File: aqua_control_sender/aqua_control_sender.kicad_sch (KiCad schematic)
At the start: 38 parts, among them J1 USB_C, J4 Conn_01x03, J5 Conn_01x03, Q2 IRLML6402, SW1 RESET, SW2 BOOT, U1 ESP32-S3-WROOM-1, U2 LM1117-3.3, U3 RA-02_LORA

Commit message: routing completed
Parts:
- removed Q2: IRLML6402, Package_TO_SOT_SMD:SOT-23, symbol Transistor_FET:IRLML6402
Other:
- note removed: "D"
- note removed: "G"
- note removed: "Protection"
- note removed: "Reverse Polarity"
- note removed: "S"
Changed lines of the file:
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@@
 	)
 	(rectangle
-		(start 106.68 144.78)
-		(end 135.89 191.77)
-		(stroke
-			(width 0)
-			(type default)
-		)
-		(fill
-			(type none)
-		)
-	)
-	(rectangle
 		(start 45.72 96.52)
 		(end 74.93 143.51)
@@
 		)
 	)
-	(text "D"
-		(exclude_from_sim no)
-		(at 116.332 172.974 0)
-		(effects
-			(font
-				(size 1.27 1.27)
-			)
-		)
-	)
 	(text "LDO SECTION"
 		(exclude_from_sim no)
@@
 		)
 	)
-	(text "Protection"
-		(exclude_from_sim no)
-		(at 114.808 149.352 0)
-		(effects
-			(font
-				(face "Aldrich")
-				(size 1.905 1.905)
-			)
-		)
-	)
-	(text "Reverse Polarity "
-		(exclude_from_sim no)
-		(at 118.364 146.812 0)
-		(effects
-			(font
-				(face "Aldrich")
-				(size 1.778 1.778)
-			)
-		)
-	)
 	(text "AQUA_CONTROL_SENDER\n"
 		(exclude_from_sim no)
@@
 		)
 	)
-	(text "S"
-		(exclude_from_sim no)
-		(at 116.332 163.322 0)
-		(effects
-			(font
-				(size 1.27 1.27)
-			)
-		)
-	)
 	(text "UART Section\n"
 		(exclude_from_sim no)
@@
 		)
 	)
-	(text "G"
-		(exclude_from_sim no)
-		(at 120.396 170.434 0)
-		(effects
-			(font
-				(size 1.27 1.27)
-			)
-		)
-	)
 	(text "JSN-SR04\n"
 		(exclude_from_sim no)
@@
 	(wire
 		(pts
-			(xy 115.57 157.48) (xy 115.57 163.83)
-		)
-		(stroke
-			(width 0)
-			(type default)
-		)
-	)
-	(wire
-		(pts
 			(xy 58.42 130.81) (xy 58.42 133.35)
 		)
@@
 	(wire
 		(pts
-			(xy 115.57 181.61) (xy 115.57 173.99)
-		)
-		(stroke
-			(width 0)
-			(type default)
-		)
-	)
-	(wire
-		(pts
 			(xy 58.42 119.38) (xy 67.31 119.38)
 		)
@@
 	(wire
 		(pts
-			(xy 125.73 168.91) (xy 123.19 168.91)
-		)
-		(stroke
-			(width 0)
-			(type default)
-		)
-	)
-	(wire
-		(pts
 			(xy 52.07 151.13) (xy 54.61 151.13)
 		)
@@
 		)
 	)
-	(global_label "5v"
-		(shape input)
-		(at 115.57 181.61 270)
-		(fields_autoplaced yes)
-		(effects
-			(font
-				(size 1.27 1.27)
-			)
-			(justify right)
-		)
-		(property "Intersheetrefs" "${INTERSHEET_REFS}"
-			(at 115.57 186.7723 90)
-			(hide yes)
-			(show_name no)
-			(do_not_autoplace no)
-			(effects
-				(font
-					(size 1.27 1.27)
-				)
-				(justify right)
-			)
-		)
-	)
 	(global_label "DIO4"
 		(shape input)
@@
 		)
 	)
-	(global_label "Vin"
-		(shape input)
-		(at 115.57 157.48 90)
-		(fields_autoplaced yes)
-		(effects
-			(font
-				(size 1.27 1.27)
-			)
-			(justify left)
-		)
-		(property "Intersheetrefs" "${INTERSHEET_REFS}"
-			(at 115.57 151.6524 90)
-			(hide yes)
-			(show_name no)
-			(do_not_autoplace no)
-			(effects
-				(font
-					(size 1.27 1.27)
-				)
-				(justify left)
-			)
-		)
-	)
 	(global_label "TX_ECHO"
 		(shape input)
@@
 		)
 	)
-	(global_label "GND"
-		(shape input)
-		(at 125.73 168.91 0)
-		(fields_autoplaced yes)
-		(effects
-			(font
-				(size 1.27 1.27)
-			)
-			(justify left)
-		)
-		(property "Intersheetrefs" "${INTERSHEET_REFS}"
-			(at 132.5857 168.91 0)
-			(hide yes)
-			(show_name no)
-			(do_not_autoplace no)
-			(effects
-				(font
-					(size 1.27 1.27)
-				)
-				(justify left)
-			)
-		)
-	)
 	(global_label "LED2"
 		(shape input)
@@
 					(unit 1)
 				)
-			)
-		)
-	)
-	(symbol
-		(lib_id "Transistor_FET:IRLML6402")
-		(at 118.11 168.91 180)
-		(unit 1)
-		(body_style 1)
-		(exclude_from_sim no)
-		(in_bom yes)
-		(on_board yes)
-		(in_pos_files yes)
-		(dnp no)
-		(property "Reference" "Q2"
-			(at 112.268 165.354 0)
-			(show_name no)
-			(do_not_autoplace no)
-			(effects
-				(font
-					(size 1.27 1.27)
-				)
-				(justify left)
-			)
-		)
-		(property "Value" "IRLML6402"
-			(at 128.778 164.338 0)
-			(show_name no)
-			(do_not_autoplace no)
-			(effects
-				(font
-					(size 1.27 1.27)
-				)
-				(justify left)
-			)
-		)
-		(property "Footprint" "Package_TO_SOT_SMD:SOT-23"
-			(at 113.03 167.005 0)
-			(hide yes)
-			(show_name no)
-			(do_not_autoplace no)
-			(effects
-				(font
-					(size 1.27 1.27)
-					(italic yes)
-				)
-				(justify left)
-			)
-		)
-		(property "Datasheet" "https://www.infineon.com/dgdl/irlml6402pbf.pdf?fileId=5546d462533600a401535668d5c2263c"
-			(at 113.03 165.1 0)
-			(hide yes)
-			(show_name no)
-			(do_not_autoplace no)
-			(effects
-				(font
-					(size 1.27 1.27)
-				)
-				(justify left)
-			)
-		)
-		(property "Description" "-3.7A Id, -20V Vds, 65mOhm Rds, P-Channel HEXFET Power MOSFET, SOT-23"
-			(at 118.11 168.91 0)
-			(hide yes)
-			(show_name no)
-			(do_not_autoplace no)
-			(effects
-				(font
-					(size 1.27 1.27)
-				)
-			)
-		)
-		(pin "1"
-		)
-		(pin "3"
-		)
-		(pin "2"
-		)
-		(instances
-			(project "aqua_control_sender"
-				(path "/8776bf0f-bc53-4fb6-b8a5-6af29be47ebb"
-					(reference "Q2")
-					(unit 1)
-				)

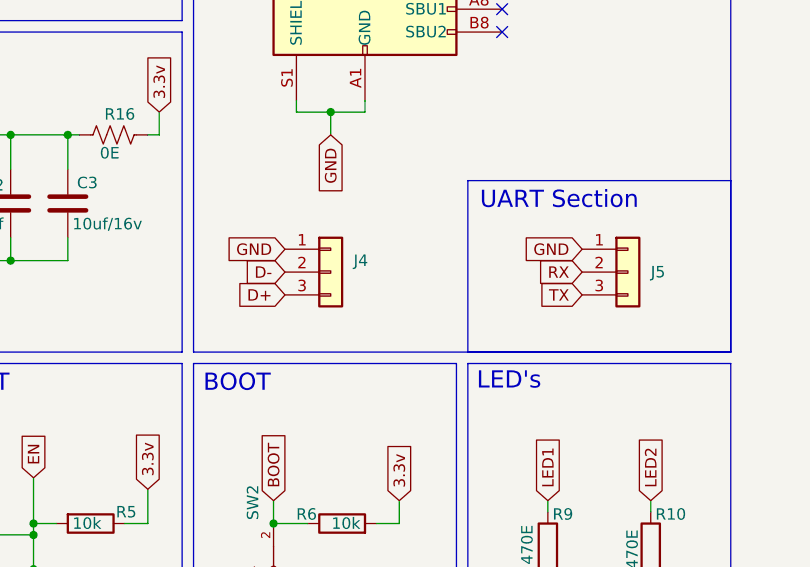
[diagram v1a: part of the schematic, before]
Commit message: completed routing and added logo
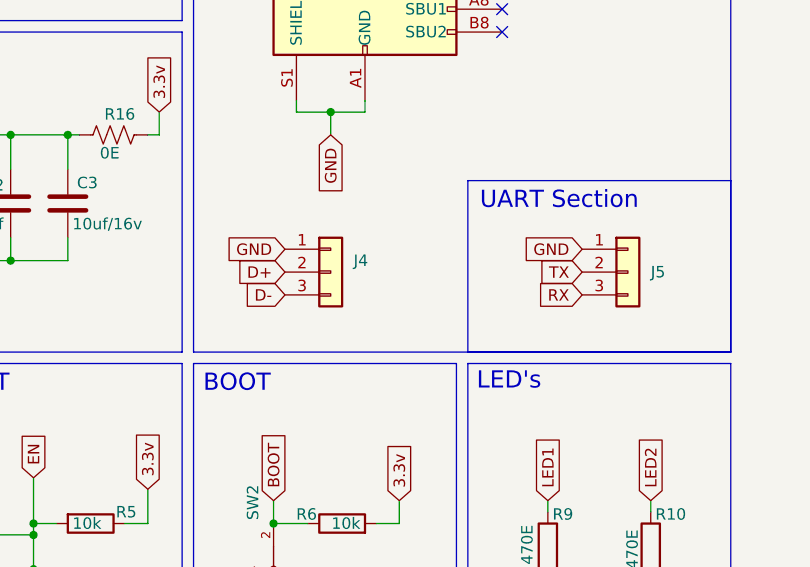
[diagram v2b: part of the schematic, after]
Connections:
- net D+: now also J4.2 (Pin_2); no longer J4.3 (Pin_3)
- net D-: now also J4.3 (Pin_3); no longer J4.2 (Pin_2)
- net RX: now also J5.3 (Pin_3); no longer J5.2 (Pin_2)
- net TX: now also J5.2 (Pin_2); no longer J5.3 (Pin_3)

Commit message: sender board complete
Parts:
- removed C4, C9: 100nf, Capacitor_SMD:C_0805_2012Metric_Pad1.18x1.45mm_HandSolder, symbol Device:C
- removed C5: 1uf, Capacitor_SMD:C_0805_2012Metric_Pad1.18x1.45mm_HandSolder, symbol Device:C
- removed C8: 47nf, Capacitor_SMD:C_0805_2012Metric_Pad1.18x1.45mm_HandSolder, symbol Device:C
- removed D3, D4: LED, LED_SMD:LED_1206_3216Metric_Pad1.42x1.75mm_HandSolder, symbol Device:LED
- removed J1: USB_C, Connector_USB:USB_C_Receptacle_GCT_USB4110, symbol Connector:USB_C_Receptacle_USB2.0_16P
- removed J4, J5: Conn_01x03, Connector_PinSocket_2.54mm:PinSocket_1x03_P2.54mm_Vertical, symbol Connector_Generic:Conn_01x03
- removed R1, R2: 5.1k, Resistor_SMD:R_0805_2012Metric_Pad1.20x1.40mm_HandSolder, symbol Device:R
- removed R10, R9: 470E, Resistor_SMD:R_0805_2012Metric_Pad1.20x1.40mm_HandSolder, symbol Device:R
- removed R5, R6, R7, R8: 10k, Resistor_SMD:R_0805_2012Metric_Pad1.20x1.40mm_HandSolder, symbol Device:R
- removed SW1: RESET, Button_Switch_THT:SW_DIP_SPSTx01_Slide_6.7x4.1mm_W7.62mm_P2.54mm_LowProfile, symbol TS09-63-25-WT-160-SMT-TR:TS09-63-25-WT-160-SMT-TR
- removed SW2: BOOT, Button_Switch_THT:SW_DIP_SPSTx01_Slide_6.7x4.1mm_W7.62mm_P2.54mm_LowProfile, symbol TS09-63-25-WT-160-SMT-TR:TS09-63-25-WT-160-SMT-TR
- removed U1: ESP32-S3-WROOM-1, RF_Module:ESP32-S3-WROOM-1, symbol RF_Module:ESP32-S3-WROOM-1
- removed U2: LM1117-3.3, Package_TO_SOT_SMD:SOT-223-3_TabPin2, symbol Regulator_Linear:AMS1117-3.3
- added C11: 100nf, Capacitor_SMD:C_0805_2012Metric_Pad1.18x1.45mm_HandSolder, symbol Device:C
- added C12: 47nf, Capacitor_SMD:C_0805_2012Metric_Pad1.18x1.45mm_HandSolder, symbol Device:C
- added D1: 1N5819WS, Diode_SMD:D_SOD-323, symbol Diode:1N5819WS
- added Q1, Q2: AO3401A, mosfet:SOT23-3, symbol AO3401A:AO3401A
- added R11, R12, R15, R18: 100k, Resistor_SMD:R_0805_2012Metric_Pad1.20x1.40mm_HandSolder, symbol Device:R
- added R13, R14: 1k, Resistor_SMD:R_0805_2012Metric_Pad1.20x1.40mm_HandSolder, symbol Device:R
- added U4: ESP32-C3_SUPERMINI_TH, esp32c3:MODULE_ESP32-C3_SUPERMINI_TH, symbol ESP32-C3_SUPERMINI_TH:ESP32-C3_SUPERMINI_TH
- added U5: MCP1700x-120xxMB, Package_TO_SOT_SMD:SOT-89-3, symbol Regulator_Linear:MCP1700x-120xxMB
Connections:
- net BAT- is gone; now on net GND: J10.3 (Pin_3), J9.2 (Pin_2)
- net 3.3v: now also C11.1, C12.1, Q1.2, U4.3.3 (3V3); no longer C6.2, C7.2, R17.2
- net BAT+: now also R11.1
- net DIO0: now also U4.2 (GPIO2)
- net GND: now also C11.2, C12.2, R12.2, U4.G (GND), U5.1 (GND)
- net MISO: now also U4.5 (GPIO5)
- net MOSI: now also U4.6 (GPIO6)
- net NSS: now also U4.7 (GPIO7)
- net RST: now also U4.3 (GPIO3)
- net RX_TRIG: now also U4.21 (GPIO21)
- net SCK: now also U4.4 (GPIO4)
- net SOL_IN+: now also D1.2 (A); no longer J10.5 (Pin_5)
- net SOL_IN-: now also R18.2
- net TX_ECHO: now also U4.20 (GPIO20)
- net at C2.1, C3.1, R16.2: now also U5.3 (VO)
- net DIO1: no longer names the net of U3.6 (DI01)
- net DIO2: no longer names the net of U3.7 (DI02)
- net DIO3: no longer names the net of U3.8 (DI03)
- net DIO4: no longer names the net of U3.10 (DI04)
- net DIO5: no longer names the net of U3.11 (DI05)
- net VCC_3V8 renamed VBAT
- net VBAT: now also Q2.2, U5.2 (VI); no longer J6.4 (Pin_4)
- new net: Q1.1, R13.2
- new net: Q2.1, R14.2
- new net BAT_IN: R11.2, R12.1, U4.1 (GPIO1)
- new net JSN_OUT: J6.4 (Pin_4), Q2.3
- new net JSN_PWR: R14.1, U4.10 (GPIO10)
- new net LORA_OUT: C6.2, C7.2, Q1.3, R17.2
- new net LORA_PWR: R13.1, U4.9 (GPIO9)
- new net SOL_IN: R15.2, R18.1, U4.0 (GPIO0)
- new net SOL_PWR+: D1.1 (K), J10.5 (Pin_5), R15.1
- no-connect marks 18 -> 8
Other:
- note added: "Charging Detection"
- note added: "D"
- note added: "ESP32C3 SECTION"
- note added: "G"
- note added: "POWER CONTROL SECTION"
- note added: "S"
- note added: "Solar Detection"
- note removed: "BOOT"
- note removed: "ESP32S3 SECTION"
- note removed: "LED's"
- note removed: "RESET"
- note removed: "STRAPPING PINS"
- note removed: "UART Section"
- note removed: "USB SECTION"
- moved on the sheet: C1, C10, C2, C3, J10, R16

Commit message: final version
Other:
- moved on the sheet: R11, R12, R15, R18
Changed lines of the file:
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@@
 	)
 	(junction
-		(at 147.32 168.91)
+		(at 147.32 167.64)
 		(diameter 0)
 		(color 0 0 0 0)
@@
 	)
 	(junction
-		(at 116.84 168.91)
+		(at 116.84 171.45)
 		(diameter 0)
 		(color 0 0 0 0)
@@
 	(wire
 		(pts
-			(xy 116.84 168.91) (xy 116.84 171.45)
+			(xy 116.84 171.45) (xy 116.84 173.99)
 		)
 		(stroke
@@
 	(wire
 		(pts
-			(xy 116.84 179.07) (xy 116.84 180.34)
+			(xy 116.84 181.61) (xy 116.84 182.88)
 		)
 		(stroke
@@
 	(wire
 		(pts
-			(xy 151.13 153.67) (xy 147.32 153.67)
+			(xy 151.13 152.4) (xy 147.32 152.4)
 		)
 		(stroke
@@
 	(wire
 		(pts
-			(xy 120.65 168.91) (xy 116.84 168.91)
+			(xy 120.65 171.45) (xy 116.84 171.45)
 		)
 		(stroke
@@
 	(wire
 		(pts
-			(xy 116.84 158.75) (xy 116.84 157.48)
+			(xy 116.84 161.29) (xy 116.84 160.02)
 		)
 		(stroke
@@
 	(wire
 		(pts
-			(xy 147.32 179.07) (xy 147.32 180.34)
+			(xy 147.32 177.8) (xy 147.32 179.07)
 		)
 		(stroke
@@
 	(wire
 		(pts
-			(xy 116.84 166.37) (xy 116.84 168.91)
+			(xy 116.84 168.91) (xy 116.84 171.45)
 		)
 		(stroke
@@
 	(wire
 		(pts
-			(xy 147.32 166.37) (xy 147.32 168.91)
+			(xy 147.32 165.1) (xy 147.32 167.64)
 		)
 		(stroke
@@
 	(wire
 		(pts
-			(xy 147.32 153.67) (xy 147.32 158.75)
+			(xy 147.32 152.4) (xy 147.32 157.48)
 		)
 		(stroke
@@
 	(wire
 		(pts
-			(xy 147.32 168.91) (xy 147.32 171.45)
+			(xy 147.32 167.64) (xy 147.32 170.18)
 		)
 		(stroke
@@
 	(wire
 		(pts
-			(xy 151.13 168.91) (xy 147.32 168.91)
+			(xy 151.13 167.64) (xy 147.32 167.64)
 		)
 		(stroke
@@
 	(global_label "SOL_PWR+"
 		(shape input)
-		(at 151.13 153.67 0)
+		(at 151.13 152.4 0)
 		(fields_autoplaced yes)
 		(effects
@@
 		)
 		(property "Intersheetrefs" "${INTERSHEET_REFS}"
-			(at 164.2147 153.67 0)
+			(at 164.2147 152.4 0)
 			(hide yes)
 			(show_name no)
@@
 	(global_label "BAT_IN"
 		(shape input)
-		(at 120.65 168.91 0)
+		(at 120.65 171.45 0)
 		(fields_autoplaced yes)
 		(effects
@@
 		)
 		(property "Intersheetrefs" "${INTERSHEET_REFS}"
-			(at 129.8643 168.91 0)
+			(at 129.8643 171.45 0)
 			(hide yes)
 			(show_name no)
@@
 	(global_label "GND"
 		(shape input)
-		(at 116.84 180.34 270)
+		(at 116.84 182.88 270)
 		(fields_autoplaced yes)
 		(effects
@@
 		)
 		(property "Intersheetrefs" "${INTERSHEET_REFS}"
-			(at 116.84 187.1957 90)
+			(at 116.84 189.7357 90)
 			(hide yes)
 			(show_name no)
@@
 	(global_label "SOL_IN"
 		(shape input)
-		(at 151.13 168.91 0)
+		(at 151.13 167.64 0)
 		(fields_autoplaced yes)
 		(effects
@@
 		)
 		(property "Intersheetrefs" "${INTERSHEET_REFS}"
-			(at 160.5862 168.91 0)
+			(at 160.5862 167.64 0)
 			(hide yes)
 			(show_name no)
@@
 	(global_label "SOL_IN-"
 		(shape input)
-		(at 147.32 180.34 270)
+		(at 147.32 179.07 270)
 		(fields_autoplaced yes)
 		(effects
@@
 		)
 		(property "Intersheetrefs" "${INTERSHEET_REFS}"
-			(at 147.32 191.3686 90)
+			(at 147.32 190.0986 90)
 			(hide yes)
 			(show_name no)
@@
 	(global_label "BAT+"
 		(shape input)
-		(at 116.84 157.48 90)
+		(at 116.84 160.02 90)
 		(fields_autoplaced yes)
 		(effects
@@
 		)
 		(property "Intersheetrefs" "${INTERSHEET_REFS}"
-			(at 116.84 149.5962 90)
+			(at 116.84 152.1362 90)
 			(hide yes)
 			(show_name no)
@@
 	(symbol
 		(lib_id "Device:R")
-		(at 147.32 162.56 0)
+		(at 147.32 161.29 0)
 		(unit 1)
 		(body_style 1)
@@
 		(dnp no)
 		(property "Reference" "R15"
-			(at 147.828 159.004 0)
+			(at 147.828 157.734 0)
 			(show_name no)
 			(do_not_autoplace no)
@@
 		)
 		(property "Value" "100k"
-			(at 145.034 164.592 90)
+			(at 145.034 163.322 90)
 			(show_name no)
 			(do_not_autoplace no)
@@
 		)
 		(property "Footprint" "Resistor_SMD:R_0805_2012Metric_Pad1.20x1.40mm_HandSolder"
-			(at 145.542 162.56 90)
+			(at 145.542 161.29 90)
 			(hide yes)
 			(show_name no)
@@
 		)
 		(property "Datasheet" ""
-			(at 147.32 162.56 0)
+			(at 147.32 161.29 0)
 			(hide yes)
 			(show_name no)
@@
 		)
 		(property "Description" "Resistor"
-			(at 147.32 162.56 0)
+			(at 147.32 161.29 0)
 			(hide yes)
 			(show_name no)
@@
 	(symbol
 		(lib_id "Device:R")
-		(at 147.32 175.26 0)
+		(at 147.32 173.99 0)
 		(unit 1)
 		(body_style 1)
@@
 		(dnp no)
 		(property "Reference" "R18"
-			(at 147.828 171.704 0)
+			(at 147.828 170.434 0)
 			(show_name no)
 			(do_not_autoplace no)
@@
 		)
 		(property "Value" "100k"
-			(at 145.288 177.8 90)
+			(at 145.288 176.53 90)
 			(show_name no)
 			(do_not_autoplace no)
@@
 		)
 		(property "Footprint" "Resistor_SMD:R_0805_2012Metric_Pad1.20x1.40mm_HandSolder"
-			(at 145.542 175.26 90)
+			(at 145.542 173.99 90)
 			(hide yes)
 			(show_name no)
@@
 		)
 		(property "Datasheet" ""
-			(at 147.32 175.26 0)
+			(at 147.32 173.99 0)
 			(hide yes)
 			(show_name no)
@@
 		)
 		(property "Description" "Resistor"
-			(at 147.32 175.26 0)
+			(at 147.32 173.99 0)
 			(hide yes)
 			(show_name no)
@@
 	(symbol
 		(lib_id "Device:R")
-		(at 116.84 162.56 0)
+		(at 116.84 165.1 0)
 		(unit 1)
 		(body_style 1)
@@
 		(dnp no)
 		(property "Reference" "R11"
-			(at 117.348 159.004 0)
+			(at 117.348 161.544 0)
 			(show_name no)
 			(do_not_autoplace no)
@@
 		)
 		(property "Value" "100k"
-			(at 114.554 164.592 90)
+			(at 114.554 167.132 90)
 			(show_name no)
 			(do_not_autoplace no)
@@
 		)
 		(property "Footprint" "Resistor_SMD:R_0805_2012Metric_Pad1.20x1.40mm_HandSolder"
-			(at 115.062 162.56 90)
+			(at 115.062 165.1 90)
 			(hide yes)
 			(show_name no)
@@
 		)
 		(property "Datasheet" ""
-			(at 116.84 162.56 0)
+			(at 116.84 165.1 0)
 			(hide yes)
 			(show_name no)
@@
 		)
 		(property "Description" "Resistor"
-			(at 116.84 162.56 0)
+			(at 116.84 165.1 0)
 			(hide yes)
 			(show_name no)
@@
 	(symbol
 		(lib_id "Device:R")
-		(at 116.84 175.26 0)
+		(at 116.84 177.8 0)
 		(unit 1)
 		(body_style 1)
@@
 		(dnp no)
 		(property "Reference" "R12"
-			(at 117.348 171.704 0)
+			(at 117.348 174.244 0)
 			(show_name no)
 			(do_not_autoplace no)
@@
 		)
 		(property "Value" "100k"
-			(at 114.808 177.8 90)
+			(at 114.808 180.34 90)
 			(show_name no)
 			(do_not_autoplace no)
@@
 		)
 		(property "Footprint" "Resistor_SMD:R_0805_2012Metric_Pad1.20x1.40mm_HandSolder"
-			(at 115.062 175.26 90)
+			(at 115.062 177.8 90)
 			(hide yes)
 			(show_name no)
@@
 		)
 		(property "Datasheet" ""
-			(at 116.84 175.26 0)
+			(at 116.84 177.8 0)
 			(hide yes)
 			(show_name no)
@@
 		)
 		(property "Description" "Resistor"
-			(at 116.84 175.26 0)
+			(at 116.84 177.8 0)
 			(hide yes)
 			(show_name no)
